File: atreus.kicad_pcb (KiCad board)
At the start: 2 copper layers, 232 x 90 mm, 85 parts

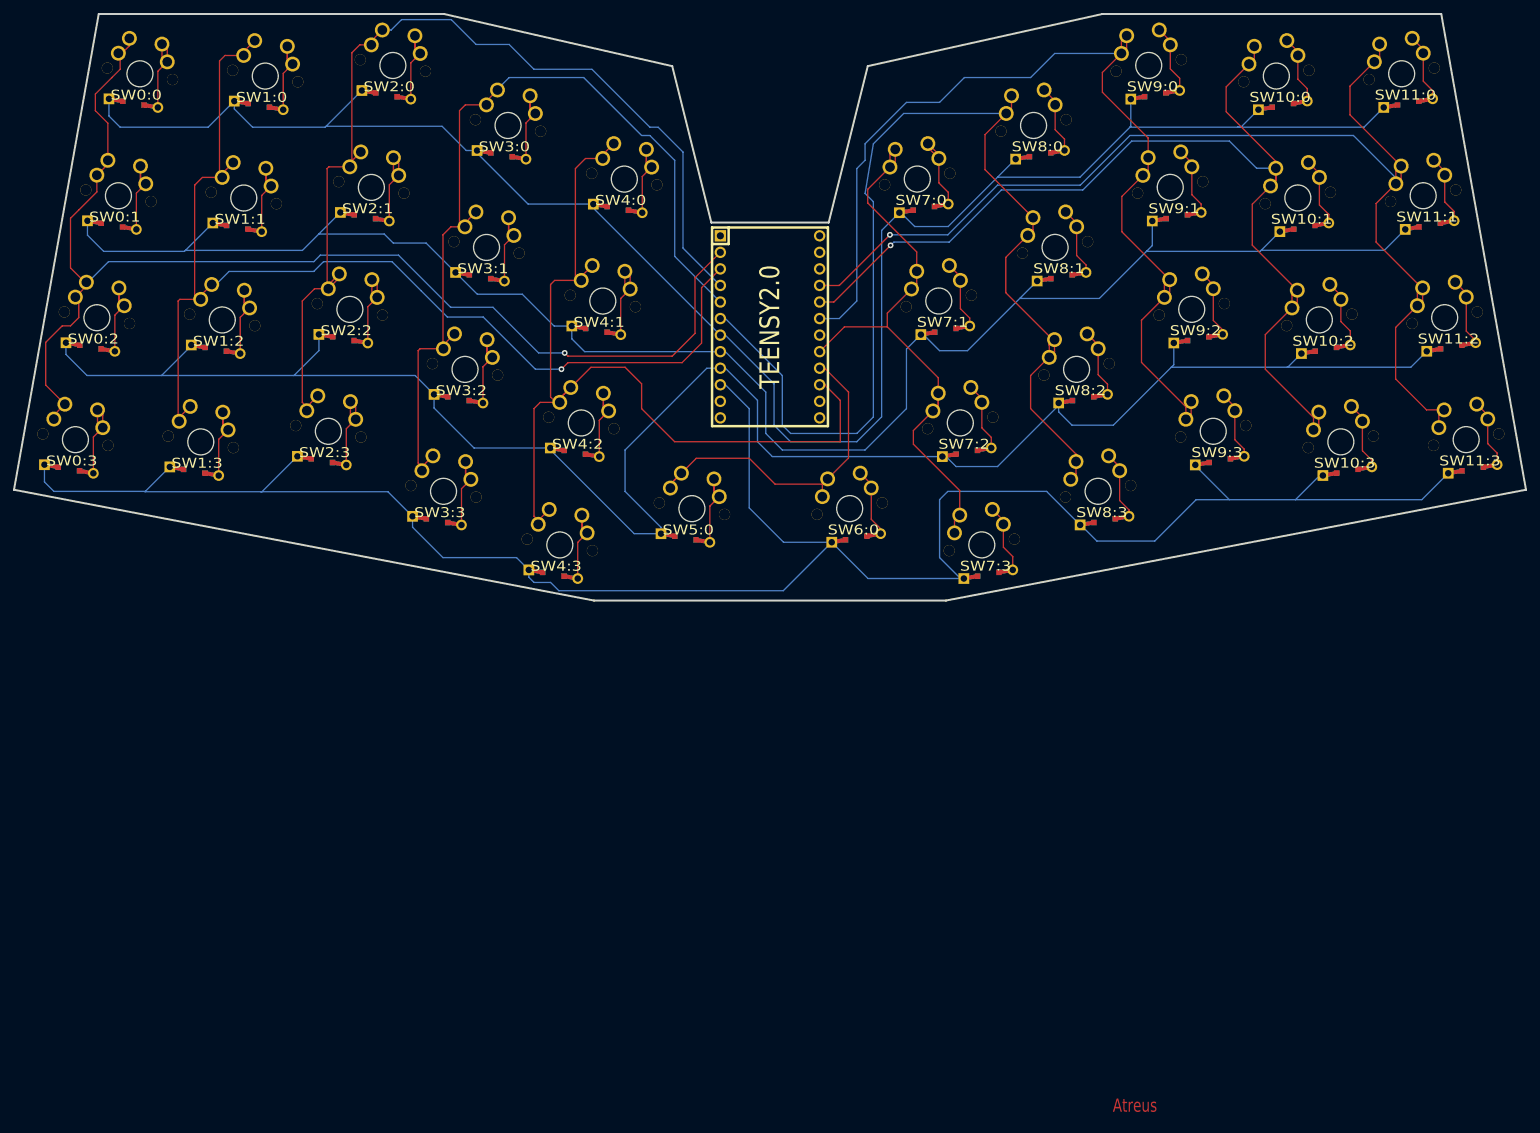
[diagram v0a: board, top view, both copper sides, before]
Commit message: Retrace with moved diodes; add silkscreening.
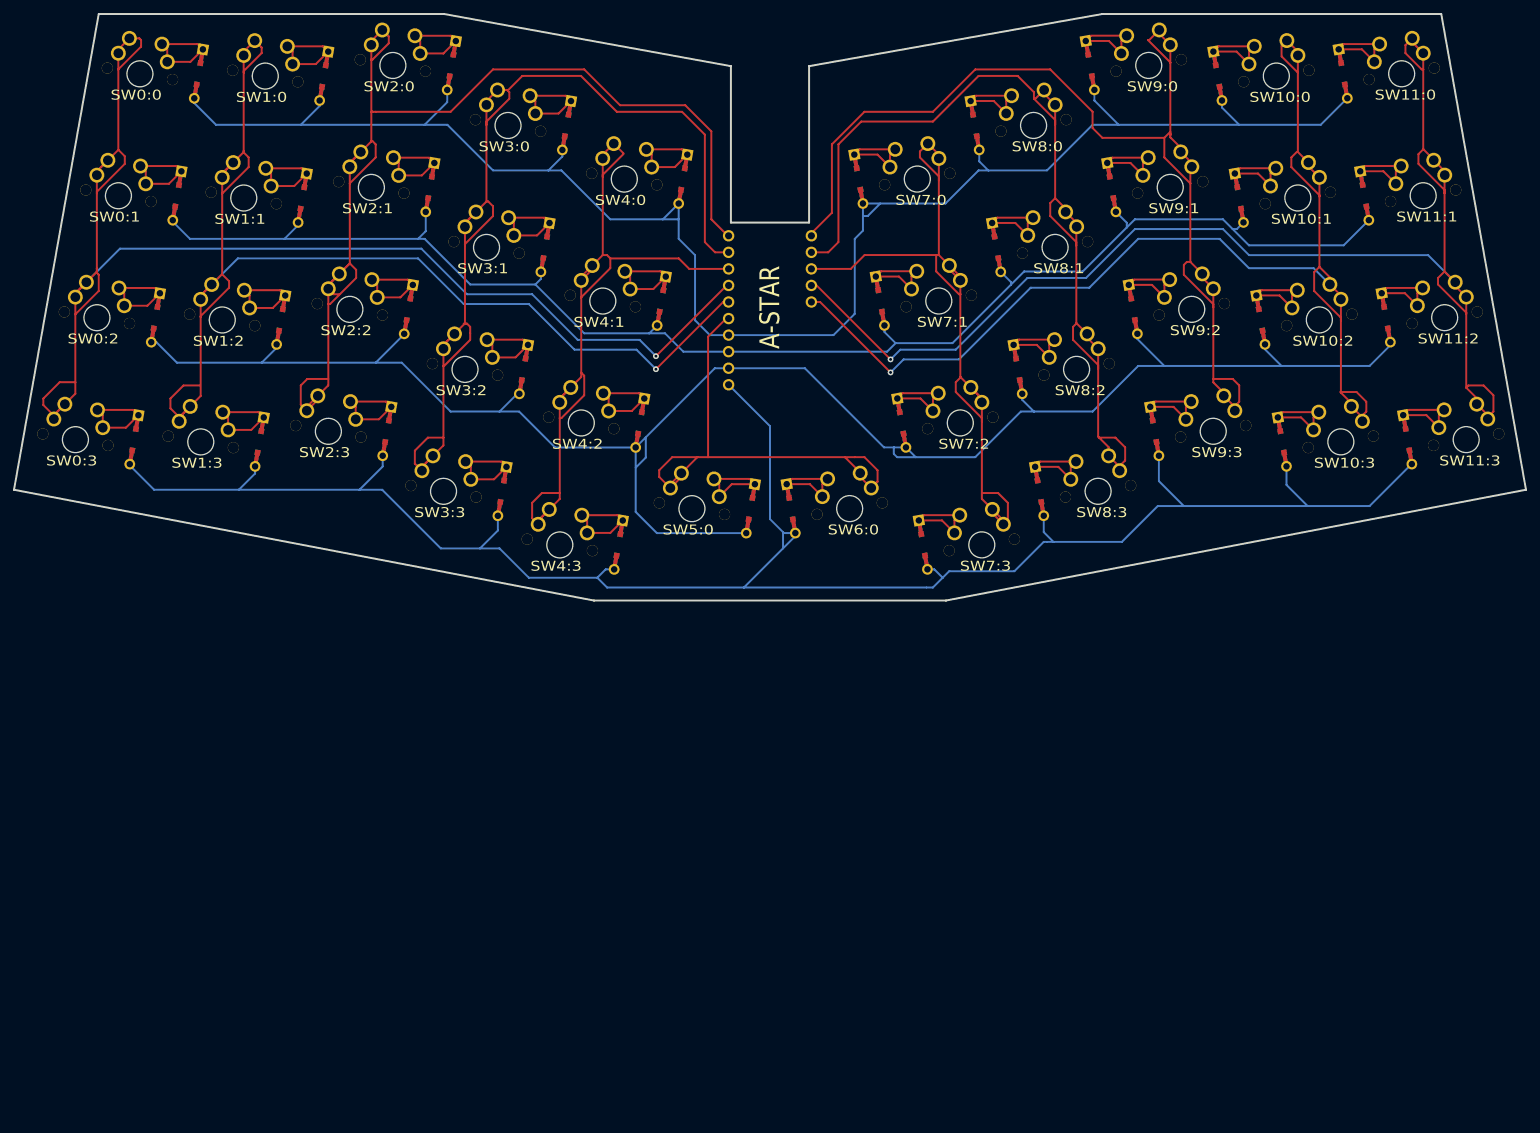
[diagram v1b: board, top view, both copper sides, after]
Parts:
- removed the D2:2 at (36.3, 35.7)
- removed the D2:2 at (71.8, 53.1)
- removed the D2:2 at (68.5, 71.8)
- removed the D2:2 at (65.2, 90.5)
- removed the D2:2 at (92.8, 43.6)
- removed the D2:2 at (89.5, 62.3)
- removed the D2:2 at (86.2, 81.0)
- removed the D2:2 at (82.9, 99.7)
- removed the D2:2 at (110.6, 51.8)
- removed the D2:2 at (107.3, 70.5)
- removed the D2:2 at (104.0, 89.3)
- removed the D2:2 at (33.0, 54.4)
- removed the D2:2 at (100.7, 108.0)
- removed the D2:2 at (121.0, 102.4)
- removed the D2:2 at (147.2, 102.4)
- removed the D2:2 at (157.6, 51.8)
- removed the D2:2 at (160.9, 70.5)
- removed the D2:2 at (164.2, 89.2)
- removed the D2:2 at (167.5, 108.0)
- removed the D2:2 at (175.4, 43.6)
- removed the D2:2 at (178.7, 62.3)
- removed the D2:2 at (182.0, 81.0)
- removed the D2:2 at (29.7, 73.1)
- removed the D2:2 at (185.3, 99.7)
- removed the D2:2 at (193.1, 34.4)
- removed the D2:2 at (196.4, 53.1)
- removed the D2:2 at (199.7, 71.8)
- removed the D2:2 at (203.0, 90.5)
- removed the D2:2 at (212.7, 36.0)
- removed the D2:2 at (216.0, 54.7)
- removed the D2:2 at (219.3, 73.4)
- removed the D2:2 at (222.6, 92.2)
- removed the D2:2 at (231.9, 35.7)
- removed the D2:2 at (26.4, 91.8)
- removed the D2:2 at (235.2, 54.4)
- removed the D2:2 at (238.5, 73.1)
- removed the D2:2 at (241.8, 91.8)
- removed the D2:2 at (55.6, 36.0)
- removed the D2:2 at (52.3, 54.7)
- removed the D2:2 at (49.0, 73.4)
- removed the D2:2 at (45.7, 92.2)
- removed the D2:2 at (75.1, 34.4)
- added D2:2: , DIODE, F.Cu at (46.3, 31.2)
- added D2:2: , DIODE, F.Cu at (81.8, 48.6)
- added D2:2: , DIODE, F.Cu at (78.5, 67.3)
- added D2:2: , DIODE, F.Cu at (75.2, 86.0)
- added D2:2: , DIODE, F.Cu at (102.8, 39.1)
- added D2:2: , DIODE, F.Cu at (99.5, 57.8)
- added D2:2: , DIODE, F.Cu at (96.2, 76.5)
- added D2:2: , DIODE, F.Cu at (92.9, 95.2)
- added D2:2: , DIODE, F.Cu at (120.6, 47.3)
- added D2:2: , DIODE, F.Cu at (117.3, 66.0)
- added D2:2: , DIODE, F.Cu at (114.0, 84.8)
- added D2:2: , DIODE, F.Cu at (43.0, 49.9)
- added D2:2: , DIODE, F.Cu at (110.7, 103.5)
- added D2:2: , DIODE, F.Cu at (131.0, 97.9)
- added D2:2: , DIODE, F.Cu at (137.2, 97.9)
- added D2:2: , DIODE, F.Cu at (147.6, 47.3)
- added D2:2: , DIODE, F.Cu at (150.9, 66.0)
- added D2:2: , DIODE, F.Cu at (154.2, 84.7)
- added D2:2: , DIODE, F.Cu at (157.5, 103.5)
- added D2:2: , DIODE, F.Cu at (165.4, 39.1)
- added D2:2: , DIODE, F.Cu at (168.7, 57.8)
- added D2:2: , DIODE, F.Cu at (172.0, 76.5)
- added D2:2: , DIODE, F.Cu at (39.7, 68.6)
- added D2:2: , DIODE, F.Cu at (175.3, 95.2)
- added D2:2: , DIODE, F.Cu at (183.1, 29.9)
- added D2:2: , DIODE, F.Cu at (186.4, 48.6)
- added D2:2: , DIODE, F.Cu at (189.7, 67.3)
- added D2:2: , DIODE, F.Cu at (193.0, 86.0)
- added D2:2: , DIODE, F.Cu at (202.7, 31.5)
- added D2:2: , DIODE, F.Cu at (206.0, 50.2)
- added D2:2: , DIODE, F.Cu at (209.3, 68.9)
- added D2:2: , DIODE, F.Cu at (212.6, 87.7)
- added D2:2: , DIODE, F.Cu at (221.9, 31.2)
- added D2:2: , DIODE, F.Cu at (36.4, 87.3)
- added D2:2: , DIODE, F.Cu at (225.2, 49.9)
- added D2:2: , DIODE, F.Cu at (228.5, 68.6)
- added D2:2: , DIODE, F.Cu at (231.8, 87.3)
- added D2:2: , DIODE, F.Cu at (65.6, 31.5)
- added D2:2: , DIODE, F.Cu at (62.3, 50.2)
- added D2:2: , DIODE, F.Cu at (59.0, 68.9)
- added D2:2: , DIODE, F.Cu at (55.7, 87.7)
- added D2:2: , DIODE, F.Cu at (85.1, 29.9)
- ?: value TEENSY2.0 -> A-STAR; footprint TEENSY_2.0 -> A_STAR
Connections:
- ? pad B4: N-col-4 -> N-col-3
- ? pad B5: N-col-5 -> N-col-2
- ? pad B7: N-col-7 -> N-col-10
- ? pad C6: (no net) -> N-col-1
- ? pad D2: N-row-2 -> N-row-3
- ? pad D3: N-row-3 -> N-row-2
- ? pad D6: (no net) -> N-col-9
- ? pad D7: (no net) -> N-col-0
- ? pad F6: N-col-8 -> N-col-7
- ? pad F7: (no net) -> N-col-8
- SW10:0 pad 1: N-diode-40 -> N-col-9
- SW10:0 pad 2: N-col-9 -> N-diode-40
- SW10:1 pad 1: N-diode-41 -> N-col-9
- SW10:1 pad 2: N-col-9 -> N-diode-41
- SW10:2 pad 1: N-diode-21 -> N-col-9
- SW10:2 pad 2: N-col-9 -> N-diode-21
- SW10:3 pad 1: N-diode-22 -> N-col-9
- SW10:3 pad 2: N-col-9 -> N-diode-22
- SW11:0 pad 1: N-diode-23 -> N-col-10
- SW11:0 pad 2: N-col-10 -> N-diode-23
- SW11:1 pad 1: N-diode-25 -> N-col-10
- SW11:1 pad 2: N-col-10 -> N-diode-25
- SW11:2 pad 1: N-diode-26 -> N-col-10
- SW11:2 pad 2: N-col-10 -> N-diode-26
- SW11:3 pad 1: N-diode-27 -> N-col-10
- SW11:3 pad 2: N-col-10 -> N-diode-27
- SW6:0 pad 1: N-diode-24 -> N-col-5
- SW6:0 pad 2: N-col-5 -> N-diode-24
- SW7:0 pad 1: N-diode-28 -> N-col-6
- SW7:0 pad 2: N-col-6 -> N-diode-28
- SW7:1 pad 1: N-diode-29 -> N-col-6
- SW7:1 pad 2: N-col-6 -> N-diode-29
- SW7:2 pad 1: N-diode-30 -> N-col-6
- SW7:2 pad 2: N-col-6 -> N-diode-30
- SW7:3 pad 1: N-diode-31 -> N-col-6
- SW7:3 pad 2: N-col-6 -> N-diode-31
- SW8:0 pad 1: N-diode-32 -> N-col-7
- SW8:0 pad 2: N-col-7 -> N-diode-32
- SW8:1 pad 1: N-diode-33 -> N-col-7
- SW8:1 pad 2: N-col-7 -> N-diode-33
- SW8:2 pad 1: N-diode-34 -> N-col-7
- SW8:2 pad 2: N-col-7 -> N-diode-34
- SW8:3 pad 1: N-diode-35 -> N-col-7
- SW8:3 pad 2: N-col-7 -> N-diode-35
- SW9:0 pad 1: N-diode-36 -> N-col-8
- SW9:0 pad 2: N-col-8 -> N-diode-36
- SW9:1 pad 1: N-diode-37 -> N-col-8
- SW9:1 pad 2: N-col-8 -> N-diode-37
- SW9:2 pad 1: N-diode-38 -> N-col-8
- SW9:2 pad 2: N-col-8 -> N-diode-38
- SW9:3 pad 1: N-diode-39 -> N-col-8
- SW9:3 pad 2: N-col-8 -> N-diode-39
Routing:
- net N-row-1: track 270.3 -> 226.9 mm
- net N-col-2: track 156.3 -> 189.2 mm
- net N-col-6: track 92.9 -> 124.5 mm
- net N-col-0: track 187.2 -> 218.7 mm
- net N-col-7: track 182.7 -> 153.6 mm
- net N-col-3: track 134.4 -> 162.6 mm
- net N-col-10: track 184.0 -> 211.5 mm
- net N-col-9: track 165.5 -> 193.0 mm
- net N-col-5: track 54.4 -> 80.4 mm
- net N-row-0: track 288.7 -> 264.8 mm
- net N-col-1: track 174.0 -> 197.0 mm
- net N-row-3: track 320.2 -> 299.5 mm
- net N-col-8: track 159.5 -> 176.2 mm
- net N-col-4: track 140.2 -> 124.1 mm
- net N-row-2: track 291.7 -> 281.8 mm
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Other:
- outline, holes or cut-outs redrawn
- board text removed: "Atreus"
